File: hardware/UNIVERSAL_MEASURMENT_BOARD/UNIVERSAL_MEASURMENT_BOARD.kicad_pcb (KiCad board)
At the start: 2 copper layers, 68 parts, among them J10 2604-1104, J2 2606-1110_010-000, U1 ADS8863IDGS, U10 TPS54202HDDCR, U12 TPS54202HDDCR, U13 L7805ABD2T-TR, U14 ADM3055EBRIZ-RL, U15 TLV76133KVUR, U16 TLV76133KVUR, U2 LT3471EDD#PBF, U3 CD4067BM96, U4 PGA280AIPW, U5 CD4067BM96, U6 STM32G484RET3, U7 L7812ABD2T-TR, U8 MC7815BDTRKG, Y1 ECS-1612MV

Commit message: final schematic review corrections
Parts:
- removed D41, D46: 3.6V/400W, Package_TO_SOT_SMD:SOT-23-6
- removed D43: BZX84C5V6, Package_TO_SOT_SMD:SOT-23
- removed D45: BZX84C3V6-E3-08, Package_TO_SOT_SMD:SOT-23
- removed J10: 2604-1104, 2604-1104:26041104
- added C11: 100nF, Capacitor_SMD:C_0805_2012Metric, F.Cu at (165.4, 110.4)
- added C12: 1uF, Capacitor_SMD:C_0805_2012Metric, F.Cu at (160.2, 45.3)
- added C34: 100nF, Capacitor_SMD:C_0805_2012Metric, F.Cu at (169.1, 57.3)
- added C35: 1uF, Capacitor_SMD:C_0805_2012Metric, F.Cu at (169.1, 60.3)
- added C36: 1uF, Capacitor_SMD:C_0805_2012Metric, F.Cu at (169.1, 63.4)
- added C37: 100nF, Capacitor_SMD:C_0805_2012Metric, F.Cu at (173.5, 45.3)
- added C39: 1uF, Capacitor_SMD:C_0805_2012Metric, F.Cu at (173.5, 51.3)
- added C5: 100nF, Capacitor_SMD:C_0805_2012Metric, F.Cu at (165.4, 98.4)
- added C7: 470nF, Capacitor_SMD:C_0805_2012Metric, F.Cu at (165.4, 101.4)
- added C8: 470nF, Capacitor_SMD:C_0805_2012Metric, F.Cu at (165.4, 104.4)
- added C9: 470nF, Capacitor_SMD:C_0805_2012Metric, F.Cu at (165.4, 107.4)
- added J1: 2606-1110_010-000, 2601-1110:26011110, F.Cu at (93.3, 50.0)
- added J3: 2606-1110_010-000, 2601-1110:26011110, F.Cu at (93.3, 90.5)
- added J4: 2606-1110_010-000, 2601-1110:26011110, F.Cu at (93.3, 110.7)
- added J5: 2604-1104, 2601-1104:26011104, F.Cu at (133.7, 49.5)
- added U11: CD4097BM, CD4097BM:SOIC127P1030X265-24N, F.Cu at (156.8, 105.5)
- added U17: ESDS304DBVR, ESDS304DBVR:SOT95P280X145-5N, F.Cu at (131.6, 65.8)
- added U18: ESDS304DBVR, ESDS304DBVR:SOT95P280X145-5N, F.Cu at (131.6, 70.4)
- J2: footprint 2604-1110:26041110 -> 2601-1110:26011110
- U3: value CD4067BM96 -> MAX6063AEUR+T; footprint CD4067BM96:SOIC127P1030X265-24N -> MAX6063AEUR+T:SOT95P229X119-3N
- U5: value CD4067BM96 -> ISL21010CFH315Z-TK; footprint CD4067BM96:SOIC127P1030X265-24N -> ISL21010CFH315Z-TK:SOT95P237X112-3N
- moved U15 76.1 mm to (191.9, 48.6)
- moved U16 76.1 mm to (191.9, 58.2)
- moved U10 72.1 mm to (195.5, 87.2)
- moved U14 67.0 mm to (180.5, 126.6)
- moved C21 63.5 mm to (164.6, 48.3)
- moved C20 63.5 mm to (164.6, 45.3)
- moved C27 61.1 mm to (169.1, 45.3)
- moved C31 61.1 mm to (169.1, 51.3)
- moved C28 61.1 mm to (169.1, 48.3)
- moved U13 60.2 mm to (180.9, 75.2)
- moved U6 58.2 mm to (181.4, 104.1)
- moved C52 57.3 mm to (177.9, 51.3)
- moved C53 57.3 mm to (177.9, 54.3)
- moved C55 57.3 mm to (177.9, 57.3)
- moved C56 57.3 mm to (177.9, 60.3)
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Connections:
- net +12VA renamed +12V0A
- net +15V renamed +15V0
- net +15VF renamed +15V0F
- net +18V renamed +18V0
- net +7V renamed +7V0
- net -18V renamed -18V0
- net /can/RX renamed /can/CAN_RX
- net /can/TX renamed /can/CAN_TX
- C16 pad 1: +15VA -> +15V0A
- C28 pad 2: -15VA -> -15V0A
- C57 pad 1: +5VA -> +5V0A
- U1 pad 1: Net-(U1-REF) -> +3V0A
- U13 pad 3: +5VA -> +5V0A
- U3 pad 1: Net-(U3-OUT) -> +5V0A
- U3 pad 2: /connectors/A8P -> +3V0A
- U3 pad 3: /connectors/A7P -> GND
- U4 pad 10: Net-(U4-INN1) -> /mux & pga/NS
- U4 pad 11: -15VA -> Net-(U4-VSN)
- U4 pad 13: +3.3VA -> Net-(U4-DVDD)
- U4 pad 3: unconnected-(U4-VOCM-Pad3) -> 1V5A
- U4 pad 4: +3.3VA -> Net-(U4-VSOP)
- U4 pad 6: +15VA -> Net-(U4-VSP)
- U4 pad 9: Net-(U3-OUT) -> /mux & pga/PS
- U5 pad 1: Net-(U4-INN1) -> +3V3A
- U5 pad 2: /connectors/A8N -> +1V5A
- U5 pad 3: /connectors/A7N -> GND
- U6 pad 28: unconnected-(U6-VREF+-Pad28) -> 3V0A
- U6 pad 30: /mcu & adc/UART_RX_PROG -> /connectors/UART_RX_PROG
- U6 pad 56: /mcu & adc/SWO -> /connectors/SWO
- U6 pad 7: /mcu & adc/NRST -> /connectors/NRST
- U6 pad 9: /mcu & adc/UART_TX_PROG -> /connectors/UART_TX_PROG
- U8 pad 3: +15VA -> +15V0A

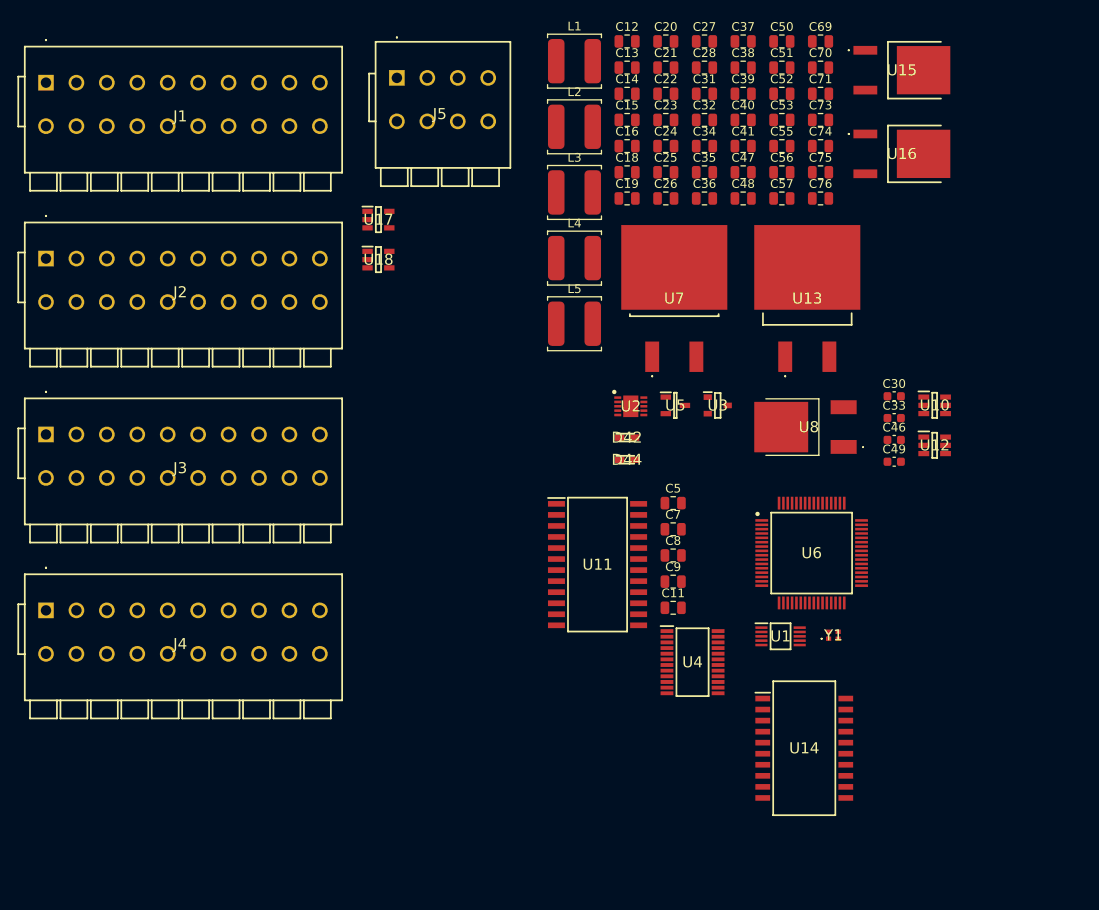
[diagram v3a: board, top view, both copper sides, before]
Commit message: added footprints
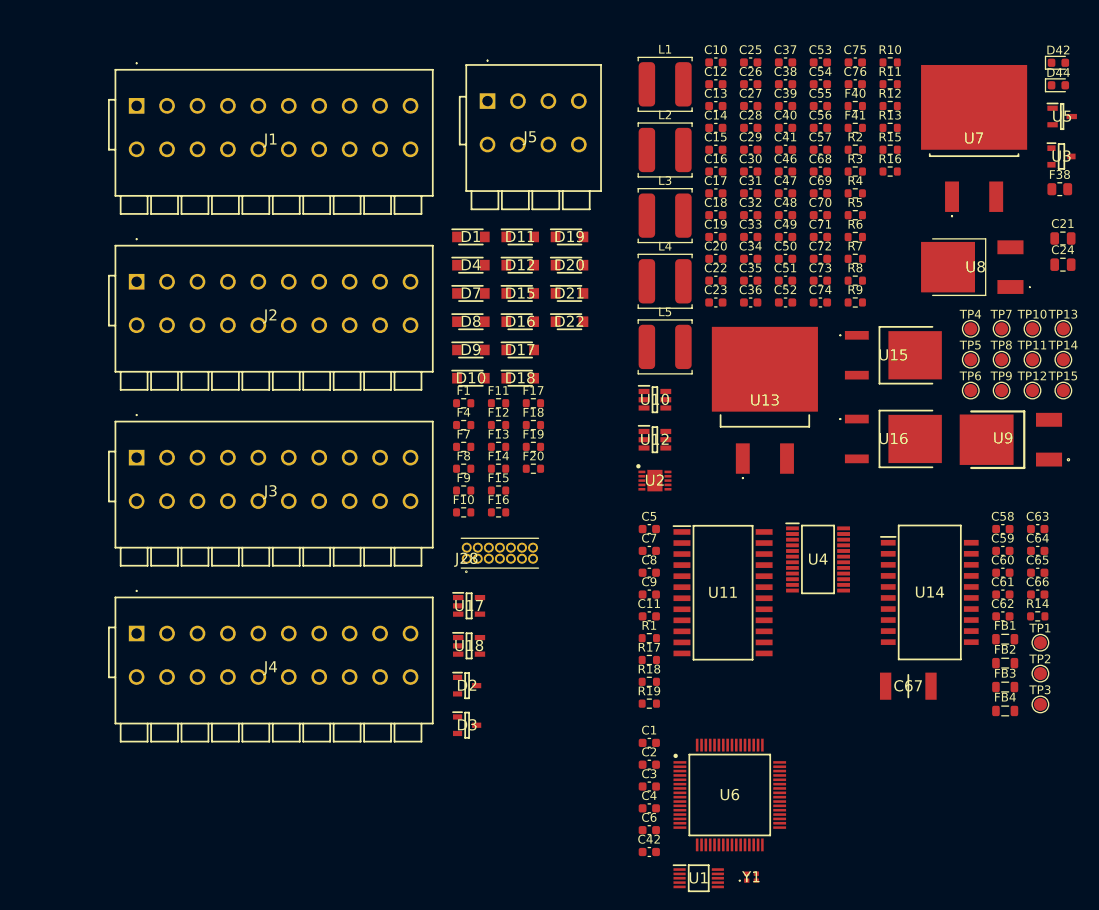
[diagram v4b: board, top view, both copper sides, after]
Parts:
- added C1: 100nF, Capacitor_SMD:C_0603_1608Metric, F.Cu at (162.7, 126.0)
- added C10: 220uF, Capacitor_SMD:C_0603_1608Metric, F.Cu at (170.4, 47.7)
- added C17: 1uF, Capacitor_SMD:C_0603_1608Metric, F.Cu at (170.4, 62.8)
- added C2: 100nF, Capacitor_SMD:C_0603_1608Metric, F.Cu at (162.7, 128.5)
- added C29: 1uF, Capacitor_SMD:C_0603_1608Metric, F.Cu at (174.4, 57.8)
- added C3: 10nF, Capacitor_SMD:C_0603_1608Metric, F.Cu at (162.7, 131.0)
- added C4: 100nF, Capacitor_SMD:C_0603_1608Metric, F.Cu at (162.7, 133.5)
- added C42: 100nF, Capacitor_SMD:C_0603_1608Metric, F.Cu at (162.7, 138.5)
- added C54: 10uF, Capacitor_SMD:C_0603_1608Metric, F.Cu at (182.4, 50.2)
- added C58: 47uF, Capacitor_SMD:C_0603_1608Metric, F.Cu at (203.4, 101.4)
- added C59: 47uF, Capacitor_SMD:C_0603_1608Metric, F.Cu at (203.4, 103.9)
- added C6: 10pF, Capacitor_SMD:C_0603_1608Metric, F.Cu at (162.7, 136.0)
- added C60: 47uF, Capacitor_SMD:C_0603_1608Metric, F.Cu at (203.4, 106.4)
- added C61: 47uF, Capacitor_SMD:C_0603_1608Metric, F.Cu at (203.4, 108.9)
- added C62: 100nF, Capacitor_SMD:C_0603_1608Metric, F.Cu at (203.4, 111.4)
- added C63: 100nF, Capacitor_SMD:C_0603_1608Metric, F.Cu at (207.4, 101.4)
- added C64: 10nF, Capacitor_SMD:C_0603_1608Metric, F.Cu at (207.4, 103.9)
- added C65: 10nF, Capacitor_SMD:C_0603_1608Metric, F.Cu at (207.4, 106.4)
- added C66: 100nF, Capacitor_SMD:C_0603_1608Metric, F.Cu at (207.4, 108.9)
- added C67: 4.7nF/Y2, S252B222K502CT:CAPC5728X280N, F.Cu at (192.5, 119.5)
- added C68: 10uF, Capacitor_SMD:C_0603_1608Metric, F.Cu at (182.4, 60.3)
- added C72: 10uF, Capacitor_SMD:C_0603_1608Metric, F.Cu at (182.4, 70.3)
- added D1: ATV02W150-HF, ATV02W150-HF:SODFL3718X130N, F.Cu at (142.2, 67.8)
- added D10: ATV02W150-HF, ATV02W150-HF:SODFL3718X130N, F.Cu at (142.2, 84.0)
- added D11: ATV02W150-HF, ATV02W150-HF:SODFL3718X130N, F.Cu at (147.9, 67.8)
- added D12: ATV02W150-HF, ATV02W150-HF:SODFL3718X130N, F.Cu at (147.9, 71.0)
- added D15: ATV02W150-HF, ATV02W150-HF:SODFL3718X130N, F.Cu at (147.9, 74.3)
- added D16: ATV02W150-HF, ATV02W150-HF:SODFL3718X130N, F.Cu at (147.9, 77.5)
- added D17: ATV02W150-HF, ATV02W150-HF:SODFL3718X130N, F.Cu at (147.9, 80.8)
- added D18: ATV02W150-HF, ATV02W150-HF:SODFL3718X130N, F.Cu at (147.9, 84.0)
- added D19: ATV02W150-HF, ATV02W150-HF:SODFL3718X130N, F.Cu at (153.5, 67.8)
- added D2: PESD5V0L2BT,215, PESD5V0L2BT,215:SOT95P230X110-3N, F.Cu at (141.8, 119.4)
- added D20: ATV02W150-HF, ATV02W150-HF:SODFL3718X130N, F.Cu at (153.5, 71.0)
- added D21: ATV02W150-HF, ATV02W150-HF:SODFL3718X130N, F.Cu at (153.5, 74.3)
- added D22: ATV02W150-HF, ATV02W150-HF:SODFL3718X130N, F.Cu at (153.5, 77.5)
- added D3: PESD5V0L2BT,215, PESD5V0L2BT,215:SOT95P230X110-3N, F.Cu at (141.8, 123.9)
- added D4: ATV02W150-HF, ATV02W150-HF:SODFL3718X130N, F.Cu at (142.2, 71.0)
- added D7: ATV02W150-HF, ATV02W150-HF:SODFL3718X130N, F.Cu at (142.2, 74.3)
- added D8: ATV02W150-HF, ATV02W150-HF:SODFL3718X130N, F.Cu at (142.2, 77.5)
- added D9: ATV02W150-HF, ATV02W150-HF:SODFL3718X130N, F.Cu at (142.2, 80.8)
- added F1: 100mA, Resistor_SMD:R_0603_1608Metric, F.Cu at (141.4, 86.9)
- added F10: 100mA, Resistor_SMD:R_0603_1608Metric, F.Cu at (141.4, 99.5)
- added F11: 100mA, Resistor_SMD:R_0603_1608Metric, F.Cu at (145.4, 86.9)
- added F12: 100mA, Resistor_SMD:R_0603_1608Metric, F.Cu at (145.4, 89.4)
- added F13: 100mA, Resistor_SMD:R_0603_1608Metric, F.Cu at (145.4, 91.9)
- added F14: 100mA, Resistor_SMD:R_0603_1608Metric, F.Cu at (145.4, 94.4)
- added F15: 100mA, Resistor_SMD:R_0603_1608Metric, F.Cu at (145.4, 97.0)
- added F16: 100mA, Resistor_SMD:R_0603_1608Metric, F.Cu at (145.4, 99.5)
- added F17: 100mA, Resistor_SMD:R_0603_1608Metric, F.Cu at (149.4, 86.9)
- added F18: 100mA, Resistor_SMD:R_0603_1608Metric, F.Cu at (149.4, 89.4)
- added F19: 100mA, Resistor_SMD:R_0603_1608Metric, F.Cu at (149.4, 91.9)
- added F20: 100mA, Resistor_SMD:R_0603_1608Metric, F.Cu at (149.4, 94.4)
- added F38: 1,5A, Resistor_SMD:R_0805_2012Metric, F.Cu at (209.9, 62.3)
- added F4: 100mA, Resistor_SMD:R_0603_1608Metric, F.Cu at (141.4, 89.4)
- added F40: 300mA, Resistor_SMD:R_0603_1608Metric, F.Cu at (186.4, 52.7)
- added F41: 300mA, Resistor_SMD:R_0603_1608Metric, F.Cu at (186.4, 55.2)
- added F7: 100mA, Resistor_SMD:R_0603_1608Metric, F.Cu at (141.4, 91.9)
- added F8: 100mA, Resistor_SMD:R_0603_1608Metric, F.Cu at (141.4, 94.4)
- added F9: 100mA, Resistor_SMD:R_0603_1608Metric, F.Cu at (141.4, 97.0)
- added FB1: 2K@100MHz, Inductor_SMD:L_0805_2012Metric, F.Cu at (203.6, 114.0)
- added FB2: 2K@100MHz, Inductor_SMD:L_0805_2012Metric, F.Cu at (203.6, 116.8)
- added FB3: 2K@100MHz, Inductor_SMD:L_0805_2012Metric, F.Cu at (203.6, 119.5)
- added FB4: 2K@100MHz, Inductor_SMD:L_0805_2012Metric, F.Cu at (203.6, 122.3)
- added J28: FTSH-107-01-L-D-K, FTSH-107-01-L-D-K:FTSH-107-XX-YYY-D-K, F.Cu at (141.7, 104.8)
- added R1: 22R, Resistor_SMD:R_0603_1608Metric, F.Cu at (162.7, 113.9)
- added R10: 649kR, Resistor_SMD:R_0603_1608Metric, F.Cu at (190.4, 47.7)
- added R11: 243kR, Resistor_SMD:R_0603_1608Metric, F.Cu at (190.4, 50.2)
- added R12: 64.9kR, Resistor_SMD:R_0603_1608Metric, F.Cu at (190.4, 52.7)
- added R13: 10kR, Resistor_SMD:R_0603_1608Metric, F.Cu at (190.4, 55.2)
- added R14: 100kR, Resistor_SMD:R_0603_1608Metric, F.Cu at (207.4, 111.4)
- added R15: 15kR, Resistor_SMD:R_0603_1608Metric, F.Cu at (190.4, 57.8)
- added R16: 274kR, Resistor_SMD:R_0603_1608Metric, F.Cu at (190.4, 60.3)
- added R17: 22R, Resistor_SMD:R_0603_1608Metric, F.Cu at (162.7, 116.4)
- added R18: 10R, Resistor_SMD:R_0603_1608Metric, F.Cu at (162.7, 119.0)
- added R19: 10R, Resistor_SMD:R_0603_1608Metric, F.Cu at (162.7, 121.5)
- added R2: 11kR, Resistor_SMD:R_0603_1608Metric, F.Cu at (186.4, 57.8)
- added R3: 11kR, Resistor_SMD:R_0603_1608Metric, F.Cu at (186.4, 60.3)
- added R4: 255kR, Resistor_SMD:R_0603_1608Metric, F.Cu at (186.4, 62.8)
- added R5: 15kR, Resistor_SMD:R_0603_1608Metric, F.Cu at (186.4, 65.3)
- added R6: 681kR, Resistor_SMD:R_0603_1608Metric, F.Cu at (186.4, 67.8)
- added R7: -R, Resistor_SMD:R_0603_1608Metric, F.Cu at (186.4, 70.3)
- added R8: 73.2kR, Resistor_SMD:R_0603_1608Metric, F.Cu at (186.4, 72.8)
- added R9: -R, Resistor_SMD:R_0603_1608Metric, F.Cu at (186.4, 75.3)
- added TP1: C5V, TestPoint:TestPoint_Pad_D1.5mm, F.Cu at (207.7, 114.5)
- added TP10: 12VA, TestPoint:TestPoint_Pad_D1.5mm, F.Cu at (206.8, 78.3)
- added TP11: 5VA, TestPoint:TestPoint_Pad_D1.5mm, F.Cu at (206.8, 81.9)
- added TP12: 3V3A, TestPoint:TestPoint_Pad_D1.5mm, F.Cu at (206.8, 85.5)
- added TP13: 3V3, TestPoint:TestPoint_Pad_D1.5mm, F.Cu at (210.3, 78.3)
- added TP14: 3V0A, TestPoint:TestPoint_Pad_D1.5mm, F.Cu at (210.3, 81.9)
- added TP15: 1V5A, TestPoint:TestPoint_Pad_D1.5mm, F.Cu at (210.3, 85.5)
- added TP2: C3V, TestPoint:TestPoint_Pad_D1.5mm, F.Cu at (207.7, 118.0)
- added TP3: CVISO, TestPoint:TestPoint_Pad_D1.5mm, F.Cu at (207.7, 121.5)
- added TP4: M15V, TestPoint:TestPoint_Pad_D1.5mm, F.Cu at (199.7, 78.3)
- added TP5: 18V, TestPoint:TestPoint_Pad_D1.5mm, F.Cu at (199.7, 81.9)
- added TP6: -18V, TestPoint:TestPoint_Pad_D1.5mm, F.Cu at (199.7, 85.5)
- added TP7: 7V, TestPoint:TestPoint_Pad_D1.5mm, F.Cu at (203.2, 78.3)
- added TP8: 15VA, TestPoint:TestPoint_Pad_D1.5mm, F.Cu at (203.2, 81.9)
- added TP9: -15VA, TestPoint:TestPoint_Pad_D1.5mm, F.Cu at (203.2, 85.5)
- added U9: MC79M15CDTRKG, MC79M15CDTRKG:DPAK__SINGLE-GAUGE__TO-252_369C__ISSUE_F, F.Cu at (199.7, 91.1)
- C11, C12, C13, C14, C15, C16, C18, C19, C20, C22, C23, C25, C26, C27, C28, C31, C32, C34, C35, C36, C37, C38, C39, C40, C41, C47, C48, C5, C50, C51, C52, C53, C55, C56, C57, C69, C7, C70, C71, C73, C74, C75, C76, C8, C9: footprint Capacitor_SMD:C_0805_2012Metric -> Capacitor_SMD:C_0603_1608Metric
- D42, D44: footprint CDBU0340:DIOM179X85N -> Diode_SMD:D_0603_1608Metric
- moved D42 65.7 mm to (209.8, 47.8)
- moved D44 65.7 mm to (209.8, 50.3)
- moved U5 55.5 mm to (210.2, 53.9)
- moved C21 49.7 mm to (210.3, 68.0)
- moved U3 48.8 mm to (210.1, 58.5)
- moved C24 47.7 mm to (210.3, 71.0)
- moved U17 45.6 mm to (142.0, 110.2)
- moved U18 45.6 mm to (142.0, 114.8)
- moved U7 39.1 mm to (200.1, 56.2)
- moved C46 33.3 mm to (178.4, 60.3)
- moved U15 32.8 mm to (190.9, 81.4)
- moved U16 32.8 mm to (190.9, 91.0)
- moved U10 32.2 mm to (163.3, 86.5)
- moved U12 32.2 mm to (163.3, 91.1)
- moved C30 30.7 mm to (174.4, 60.3)
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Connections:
- net Net-(J5A-1.2) renamed +24V0

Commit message: first outcom of pcb design
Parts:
- removed D20, D21, D22: ATV02W150-HF, ATV02W150-HF:SODFL3718X130N
- removed D42, D44: CDBU0340, Diode_SMD:D_0603_1608Metric
- removed F20: 100mA, Resistor_SMD:R_0603_1608Metric
- removed F38: 1,5A, Resistor_SMD:R_0805_2012Metric
- removed F40, F41: 300mA, Resistor_SMD:R_0603_1608Metric
- removed J28: FTSH-107-01-L-D-K, FTSH-107-01-L-D-K:FTSH-107-XX-YYY-D-K
- removed L4: 10uH, Inductor_SMD:L_TDK_VLS6045EX_VLS6045AF
- removed L5: 15uH, Inductor_SMD:L_TDK_VLS6045EX_VLS6045AF
- removed TP13: 3V3, TestPoint:TestPoint_Pad_D1.5mm
- removed TP14: 3V0A, TestPoint:TestPoint_Pad_D1.5mm
- removed the U4 at (182.1, 104.9)
- added C43: 330nF, REST:C_0603_1608Metric, F.Cu at (94.8, 90.6)
- added C44: 330nF, REST:C_0603_1608Metric, F.Cu at (107.7, 90.6)
- added C45: 330nF, REST:C_0603_1608Metric, F.Cu at (134.0, 104.9)
- added C77: 100nF, REST:C_0603_1608Metric, F.Cu at (107.9, 137.0)
- added C78: 100nF, REST:C_0603_1608Metric, F.Cu at (94.5, 137.0)
- added C79: 100nF, REST:C_0603_1608Metric, F.Cu at (107.9, 139.3)
- added D13: ATV02W150-HF, ATV02W150-HF:SODFL3718X130N, F.Cu at (112.8, 159.1)
- added D14: ATV02W150-HF, ATV02W150-HF:SODFL3718X130N, F.Cu at (112.8, 173.1)
- added D5: ATV02W150-HF, ATV02W150-HF:SODFL3718X130N, F.Cu at (89.7, 126.7)
- added D6: ATV02W150-HF, ATV02W150-HF:SODFL3718X130N, F.Cu at (89.7, 144.2)
- added F2: 1,5A, REST:F_0805_2012Metric, F.Cu at (94.3, 66.1)
- added F3: 300mA, REST:F_0603_1608Metric, F.Cu at (92.3, 75.1)
- added F5: 100mA, REST:F_1206_3216Metric, F.Cu at (89.7, 119.7)
- added F6: 100mA, REST:F_1206_3216Metric, F.Cu at (89.7, 133.7)
- added J6: Conn_01x01_Socket, REST:SolderWire-0.1sqmm_1x01_D0.4mm_OD1mm_Relief2x, F.Cu at (105.7, 65.8)
- added J7: Conn_01x01_Socket, REST:SolderWire-0.1sqmm_1x01_D0.4mm_OD1mm_Relief2x, F.Cu at (99.7, 65.8)
- added J8: 2606-1110_010-000, 2601-1110:26011110, F.Cu at (125.9, 167.7)
- added J9: 2606-1110_010-000, 2601-1110:26011110, F.Cu at (125.9, 131.2)
- added L6: ASPIAIG-S8050-221M-T, ASPIAIG-S8050-221M-T:INDPM8080X520N, F.Cu at (87.2, 84.2)
- added REF**: MountingHole_3.2mm_M3_Pad_Via, REST:MountingHole_3.2mm_M3_Pad_Via, F.Cu at (132.2, 193.8)
- added REF**: Screw_Generic_2.0x3.0mm_SilkScreen, Symbol:Screw_Generic_2.0x3.0mm_SilkScreen, F.Cu at (95.2, 143.8)
- added REF**: MountingHole_3.2mm_M3_Pad_Via, REST:MountingHole_3.2mm_M3_Pad_Via, F.Cu at (132.2, 66.8)
- added REF**: MountingHole_3.2mm_M3_Pad_Via, REST:MountingHole_3.2mm_M3_Pad_Via, F.Cu at (101.2, 143.8)
- added REF**: MountingHole_3.2mm_M3_Pad_Via, REST:MountingHole_3.2mm_M3_Pad_Via, F.Cu at (70.2, 193.8)
- added REF**: MountingHole_3.2mm_M3_Pad_Via, REST:MountingHole_3.2mm_M3_Pad_Via, F.Cu at (70.2, 66.8)
- added U11: L7812ABD2T-TR, L7812ABD2T-TR:L7812ABD2TTR, F.Cu at (109.2, 99.6)
- C1, C11, C19, C2, C22, C32, C38, C40, C49, C5, C6, C62, C75, C8, C9: footprint Capacitor_SMD:C_0603_1608Metric -> REST:C_0603_1608Metric
- C10: value 220uF -> 470nF; footprint Capacitor_SMD:C_0603_1608Metric -> REST:C_0603_1608Metric
- C12: value 1uF -> 10uF; footprint Capacitor_SMD:C_0603_1608Metric -> REST:C_0805_2012Metric
- C13: value 100nF -> 22uF; footprint Capacitor_SMD:C_0603_1608Metric -> REST:C_0805_2012Metric
- C14, C26, C47, C48, C50, C73, C76: value 22uF -> 100nF; footprint Capacitor_SMD:C_0603_1608Metric -> REST:C_0603_1608Metric
- C15: value 330nF -> 22uF; footprint Capacitor_SMD:C_0603_1608Metric -> REST:C_0603_1608Metric
- C16: value 220nF -> 22uF; footprint Capacitor_SMD:C_0603_1608Metric -> REST:C_0805_2012Metric
- C17, C35, C36, C39: value 1uF -> 22uF; footprint Capacitor_SMD:C_0603_1608Metric -> REST:C_0603_1608Metric
- C18, C68: value 10uF -> 100nF; footprint Capacitor_SMD:C_0603_1608Metric -> REST:C_0603_1608Metric
- C20, C23: value 1uF -> 100nF; footprint Capacitor_SMD:C_0603_1608Metric -> REST:C_0603_1608Metric
- C21: value 4.7uF -> 1uF; footprint Capacitor_SMD:C_0805_2012Metric -> REST:C_0603_1608Metric
- C24: value 10uF -> 1uF; footprint Capacitor_SMD:C_0805_2012Metric -> REST:C_0805_2012Metric
- C25: value 75pF -> 22uF; footprint Capacitor_SMD:C_0603_1608Metric -> REST:C_0805_2012Metric
- C27: value 330nF -> 75pF; footprint Capacitor_SMD:C_0603_1608Metric -> REST:C_0603_1608Metric
- C28: value 220nF -> 100nF; footprint Capacitor_SMD:C_0603_1608Metric -> REST:C_0603_1608Metric
- C29: value 1uF -> 22uF; footprint Capacitor_SMD:C_0603_1608Metric -> REST:C_0805_2012Metric
- C3: value 10nF -> 100nF; footprint Capacitor_SMD:C_0603_1608Metric -> REST:C_0603_1608Metric
- C30: value 100nF -> 10uF; footprint Capacitor_SMD:C_0603_1608Metric -> REST:C_0805_2012Metric
- C31: value 22uF -> 4.7uF; footprint Capacitor_SMD:C_0603_1608Metric -> REST:C_0805_2012Metric
- C33: value 100nF -> 220uF; footprint Capacitor_SMD:C_0603_1608Metric -> REST:CP_Elec_8x10
- C34, C37, C53: value 100nF -> 22uF; footprint Capacitor_SMD:C_0603_1608Metric -> REST:C_0603_1608Metric
- C4, C71: value 100nF -> 10nF; footprint Capacitor_SMD:C_0603_1608Metric -> REST:C_0603_1608Metric
- C41: value 22uF -> 330nF; footprint Capacitor_SMD:C_0603_1608Metric -> REST:C_0603_1608Metric
- C42, C46: value 100nF -> 330nF; footprint Capacitor_SMD:C_0603_1608Metric -> REST:C_0603_1608Metric
- C51: value 22uF -> 220nF; footprint Capacitor_SMD:C_0603_1608Metric -> REST:C_0603_1608Metric
- C52: value 330nF -> 220nF; footprint Capacitor_SMD:C_0603_1608Metric -> REST:C_0603_1608Metric
- C54: footprint Capacitor_SMD:C_0603_1608Metric -> REST:CP_Elec_4x5.8
- C55: value 22uF -> 10uF; footprint Capacitor_SMD:C_0603_1608Metric -> REST:CP_Elec_4x5.8
- C56: value 330nF -> 10uF; footprint Capacitor_SMD:C_0603_1608Metric -> REST:CP_Elec_4x5.8
- C57: value 100nF -> 1uF; footprint Capacitor_SMD:C_0603_1608Metric -> REST:CP_Elec_4x5.4
- C58: value 47uF -> 1uF; footprint Capacitor_SMD:C_0603_1608Metric -> REST:CP_Elec_4x5.4
- C59, C60: value 47uF -> 1uF; footprint Capacitor_SMD:C_0603_1608Metric -> REST:C_0603_1608Metric
- C61: value 47uF -> 100nF; footprint Capacitor_SMD:C_0603_1608Metric -> REST:C_0603_1608Metric
- C63: value 100nF -> 1uF; footprint Capacitor_SMD:C_0603_1608Metric -> REST:C_0603_1608Metric
- C64: value 10nF -> 1uF; footprint Capacitor_SMD:C_0603_1608Metric -> REST:C_0603_1608Metric
- C65: value 10nF -> 47uF; footprint Capacitor_SMD:C_0603_1608Metric -> REST:C_0603_1608Metric
- C66: value 100nF -> 47uF; footprint Capacitor_SMD:C_0603_1608Metric -> REST:C_0603_1608Metric
- C67: value 4.7nF/Y2 -> 100nF; footprint S252B222K502CT:CAPC5728X280N -> REST:C_0603_1608Metric
- C69: value 22uF -> 10nF; footprint Capacitor_SMD:C_0603_1608Metric -> REST:C_0603_1608Metric
- C7: value 470nF -> 100nF; footprint Capacitor_SMD:C_0603_1608Metric -> REST:C_0603_1608Metric
- C70: value 330nF -> 4.7nF/Y2; footprint Capacitor_SMD:C_0603_1608Metric -> S252B222K502CT:CAPC5728X280N
- C72: value 10uF -> 47uF; footprint Capacitor_SMD:C_0603_1608Metric -> REST:C_0603_1608Metric
- C74: value 330nF -> 47uF; footprint Capacitor_SMD:C_0603_1608Metric -> REST:C_0603_1608Metric
- D1: value ATV02W150-HF -> CDBU0340; footprint ATV02W150-HF:SODFL3718X130N -> REST:D_0603_1608Metric
- D11: value ATV02W150-HF -> PESD5V0L2BT,215; footprint ATV02W150-HF:SODFL3718X130N -> PESD5V0L2BT,215:SOT95P230X110-3N
- D2: value PESD5V0L2BT,215 -> CDBU0340; footprint PESD5V0L2BT,215:SOT95P230X110-3N -> REST:D_0603_1608Metric
- D3: value PESD5V0L2BT,215 -> ATV02W150-HF; footprint PESD5V0L2BT,215:SOT95P230X110-3N -> ATV02W150-HF:SODFL3718X130N
- F1: value 100mA -> 300mA; footprint Resistor_SMD:R_0603_1608Metric -> REST:F_0603_1608Metric
- F10, F11, F12, F13, F14, F15, F16, F17, F18, F19, F4, F7, F8, F9: footprint Resistor_SMD:R_0603_1608Metric -> REST:F_1206_3216Metric
- FB1, FB2, FB3, FB4: footprint Inductor_SMD:L_0805_2012Metric -> REST:L_0805_2012Metric
- J1: value 2606-1110_010-000 -> FTSH-107-01-L-D-K; footprint 2601-1110:26011110 -> FTSH-107-01-L-D-K:FTSH-107-XX-YYY-D-K
- J4: value 2606-1110_010-000 -> Conn_01x01_Socket; footprint 2601-1110:26011110 -> REST:SolderWire-0.1sqmm_1x01_D0.4mm_OD1mm_Relief2x
- J5: value 2604-1104 -> Conn_01x01_Socket; footprint 2601-1104:26011104 -> REST:SolderWire-0.1sqmm_1x01_D0.4mm_OD1mm_Relief2x
- L1: value 2.2uH -> PM3604-5-RC; footprint Inductor_SMD:L_TDK_VLS6045EX_VLS6045AF -> PM3604-5-RC:PM3604-5-RC
- L2: value 68uH/1.4A -> 74408943100; footprint Inductor_SMD:L_TDK_VLS6045EX_VLS6045AF -> 74408943100:WE-SPC_48XX78
- L3: value 68uH/1.4A -> 74437349560; footprint Inductor_SMD:L_TDK_VLS6045EX_VLS6045AF -> 74437349560:74437349560
- R1: value 22R -> 10R; footprint Resistor_SMD:R_0603_1608Metric -> REST:R_0603_1608Metric
- R10: value 649kR -> 73.2kR; footprint Resistor_SMD:R_0603_1608Metric -> REST:R_0603_1608Metric
- R11: footprint Resistor_SMD:R_0603_1608Metric -> REST:R_0603_1608Metric
- R12: value 64.9kR -> 10kR; footprint Resistor_SMD:R_0603_1608Metric -> REST:R_0603_1608Metric
- R13: value 10kR -> 255kR; footprint Resistor_SMD:R_0603_1608Metric -> REST:R_0603_1608Metric
- R14: value 100kR -> -R; footprint Resistor_SMD:R_0603_1608Metric -> REST:R_0603_1608Metric
- R15: value 15kR -> -R; footprint Resistor_SMD:R_0603_1608Metric -> REST:R_0603_1608Metric
- R16: value 274kR -> 15kR; footprint Resistor_SMD:R_0603_1608Metric -> REST:R_0603_1608Metric
- R17: value 22R -> 15kR; footprint Resistor_SMD:R_0603_1608Metric -> REST:R_0603_1608Metric
- R18: value 10R -> 274kR; footprint Resistor_SMD:R_0603_1608Metric -> REST:R_0603_1608Metric
- R19: value 10R -> 100kR; footprint Resistor_SMD:R_0603_1608Metric -> REST:R_0603_1608Metric
- R2: value 11kR -> 10R; footprint Resistor_SMD:R_0603_1608Metric -> REST:R_0603_1608Metric
- R3: value 11kR -> 22R; footprint Resistor_SMD:R_0603_1608Metric -> REST:R_0603_1608Metric
- R4: value 255kR -> 22R; footprint Resistor_SMD:R_0603_1608Metric -> REST:R_0603_1608Metric
- R5: value 15kR -> 11kR; footprint Resistor_SMD:R_0603_1608Metric -> REST:R_0603_1608Metric
- R6: value 681kR -> 649kR; footprint Resistor_SMD:R_0603_1608Metric -> REST:R_0603_1608Metric
- R7: value -R -> 681kR; footprint Resistor_SMD:R_0603_1608Metric -> REST:R_0603_1608Metric
- R8: value 73.2kR -> 64.9kR; footprint Resistor_SMD:R_0603_1608Metric -> REST:R_0603_1608Metric
- R9: value -R -> 11kR; footprint Resistor_SMD:R_0603_1608Metric -> REST:R_0603_1608Metric
- TP1: value C5V -> M15V; footprint TestPoint:TestPoint_Pad_D1.5mm -> REST:TestPoint_Pad_D1.5mm; moved to B.Cu
- TP10: value 12VA -> -15VA; footprint TestPoint:TestPoint_Pad_D1.5mm -> REST:TestPoint_Pad_D1.5mm; moved to B.Cu
- TP11: value 5VA -> 1V5A; footprint TestPoint:TestPoint_Pad_D1.5mm -> REST:TestPoint_Pad_D1.5mm; moved to B.Cu
- TP12: value 3V3A -> 3V0A; footprint TestPoint:TestPoint_Pad_D1.5mm -> REST:TestPoint_Pad_D1.5mm; moved to B.Cu
- TP15: value 1V5A -> CVISO; footprint TestPoint:TestPoint_Pad_D1.5mm -> REST:TestPoint_Pad_D1.5mm; moved to B.Cu
- TP2: value C3V -> -18V; footprint TestPoint:TestPoint_Pad_D1.5mm -> REST:TestPoint_Pad_D1.5mm; moved to B.Cu
- TP3: value CVISO -> 7V; footprint TestPoint:TestPoint_Pad_D1.5mm -> REST:TestPoint_Pad_D1.5mm; moved to B.Cu
- TP4: value M15V -> 18V; footprint TestPoint:TestPoint_Pad_D1.5mm -> REST:TestPoint_Pad_D1.5mm; moved to B.Cu
- TP5: value 18V -> 3V3; footprint TestPoint:TestPoint_Pad_D1.5mm -> REST:TestPoint_Pad_D1.5mm; moved to B.Cu
- TP6: value -18V -> 3V3A; footprint TestPoint:TestPoint_Pad_D1.5mm -> REST:TestPoint_Pad_D1.5mm; moved to B.Cu
- TP7: value 7V -> 5VA; footprint TestPoint:TestPoint_Pad_D1.5mm -> REST:TestPoint_Pad_D1.5mm; moved to B.Cu
- TP8: value 15VA -> 12VA; footprint TestPoint:TestPoint_Pad_D1.5mm -> REST:TestPoint_Pad_D1.5mm; moved to B.Cu
- TP9: value -15VA -> 15VA; footprint TestPoint:TestPoint_Pad_D1.5mm -> REST:TestPoint_Pad_D1.5mm; moved to B.Cu
- U1: value ADS8863IDGS -> STM32G484RET3; footprint ADS8863IDGS:SOP50P490X110-10N -> STM32G484RET3:QFP50P1200X1200X160-64N
- U10: value TPS54202HDDCR -> L7805ABD2T-TR; footprint TPS54202HDDCR:SOT95P280X110-6N -> L7805ABD2T-TR:L7805ABD2TTR
- U12: value TPS54202HDDCR -> L78L15ACD13TR; footprint TPS54202HDDCR:SOT95P280X110-6N -> LP358DR:SOIC127P600X175-8N
- U13: value L7805ABD2T-TR -> L79L15ACD13TR; footprint L7805ABD2T-TR:L7805ABD2TTR -> LP358DR:SOIC127P600X175-8N
- U14: value ADM3055EBRIZ-RL -> ISL21010CFH315Z-TK; footprint ADM3055EBRIZ-RL:SOIC127P1030X264-20N -> ISL21010CFH315Z-TK:SOT95P237X112-3N
- U15: value TLV76133KVUR -> ISL21010CFH330Z-TK; footprint TLV76133KVUR:TLV76133KVUR -> ISL21010CFH315Z-TK:SOT95P237X112-3N
- U16: value TLV76133KVUR -> ESDS304DBVR; footprint TLV76133KVUR:TLV76133KVUR -> ESDS304DBVR:SOT95P280X145-5N
- U18: value ESDS304DBVR -> ADM3055EBRIZ-RL; footprint ESDS304DBVR:SOT95P280X145-5N -> ADM3055EBRIZ-RL:SOIC127P1030X264-20N
- U2: value LT3471EDD#PBF -> ADS8863IDGS; footprint LT3471EDD#PBF:SON50P300X300X80-11N-D -> ADS8863IDGS:SOP50P490X110-10N
- U3: value MAX6063AEUR+T -> PGA280AIPW; footprint MAX6063AEUR+T:SOT95P229X119-3N -> PGA280AIPW:SOP65P640X120-24N
- U5: value ISL21010CFH315Z-TK -> TPS54202HDDCR; footprint ISL21010CFH315Z-TK:SOT95P237X112-3N -> TPS54202HDDCR:SOT95P280X110-6N
- U6: value STM32G484RET3 -> TPS54202HDDCR; footprint STM32G484RET3:QFP50P1200X1200X160-64N -> TPS54202HDDCR:SOT95P280X110-6N
- U7: value L7812ABD2T-TR -> LT3471EDD#PBF; footprint L7812ABD2T-TR:L7812ABD2TTR -> LT3471EDD#PBF:SON50P300X300X80-11N-D
- U8: value MC7815BDTRKG -> UA78M33CDCYRG3; footprint MC7815BDTRKG:NVD5117PLT4GVF01 -> UA78M33CDCYRG3:SOT230P700X180-4N
- U9: value MC79M15CDTRKG -> UA78M33CDCYRG3; footprint MC79M15CDTRKG:DPAK__SINGLE-GAUGE__TO-252_369C__ISSUE_F -> UA78M33CDCYRG3:SOT230P700X180-4N
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- renumbered U11 to U4
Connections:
- C10 pad 1: +15V0 -> Net-(U3-VSN)
- C11 pad 2: Net-(U4-DVDD) -> +15V0A
- C12 pad 1: +5V0A -> GND
- C12 pad 2: GND -> +15V0F
- C13 pad 2: +15V0F -> Net-(U5-VIN)
- C14 pad 1: +18V0 -> GND
- C14 pad 2: GND -> +15V0F
- C15 pad 1: +18V0 -> GND
- C15 pad 2: GND -> Net-(U6-VIN)
- C16 pad 1: +15V0A -> GND
- C16 pad 2: GND -> Net-(U5-VIN)
- C17 pad 1: +15V0A -> GND
- C17 pad 2: GND -> Net-(U6-VIN)
- C18 pad 2: +15V0F -> Net-(U5-VIN)
- C19 pad 2: Net-(U2-~{SHDN}/SS1) -> Net-(U7-~{SHDN}/SS1)
- C2 pad 1: +3V3A -> +3V3
- C20 pad 2: Net-(U2-~{SHDN}/SS2) -> Net-(U6-VIN)
- C21 pad 2: +18V0 -> Net-(U7-~{SHDN}/SS2)
- C22 pad 1: GND -> Net-(U5-BOOT)
- C22 pad 2: Net-(U2-FB1P) -> Net-(U5-SW)
- C23 pad 1: Net-(D44-A) -> Net-(U6-BOOT)
- C23 pad 2: Net-(U2-SW2) -> Net-(U6-SW)
- C24 pad 1: GND -> Net-(D2-A)
- C24 pad 2: -18V0 -> Net-(U7-SW2)
- C25 pad 1: -18V0 -> +15V0
- C25 pad 2: Net-(U2-FB2P) -> GND
- C26 pad 2: -18V0 -> Net-(U7-FB1P)
- C27 pad 1: GND -> -18V0
- C27 pad 2: -18V0 -> Net-(U7-FB2P)
- C28 pad 1: GND -> +7V0
- C28 pad 2: -15V0A -> GND
- C29 pad 1: GND -> +15V0
- C29 pad 2: -15V0A -> GND
- C30 pad 1: Net-(U10-BOOT) -> GND
- C30 pad 2: Net-(U10-SW) -> -18V0
- C31 pad 2: Net-(U10-VIN) -> +18V0
- C32 pad 1: GND -> +7V0
- C32 pad 2: Net-(U10-VIN) -> GND
- C33 pad 1: GND -> +15V0
- C33 pad 2: Net-(U10-VIN) -> GND
- C34 pad 1: +1V5A -> +7V0
- C35 pad 1: +1V5A -> +7V0
- C36 pad 1: +3V3A -> +7V0
- C37 pad 1: +3V0A -> +7V0
- C38 pad 1: +7V0 -> +15V0
- C39 pad 1: +3V0A -> +18V0
- C4 pad 1: +3V0A -> +3V3A
- C40 pad 1: +15V0 -> GND
- C40 pad 2: GND -> -18V0
- C42 pad 1: +3V3 -> +7V0
- C46 pad 1: Net-(U12-BOOT) -> GND
- C46 pad 2: Net-(U12-SW) -> -18V0
- C47 pad 1: GND -> +3V3
- C47 pad 2: Net-(U12-VIN) -> GND
- C48 pad 1: GND -> +3V3A
- C48 pad 2: Net-(U12-VIN) -> GND
- C49 pad 1: GND -> +5V0A
- C49 pad 2: Net-(U12-VIN) -> GND
- C5 pad 1: GND -> +3V0A
- C5 pad 2: +15V0A -> GND
- C50 pad 1: +15V0 -> +12V0A
- C51 pad 1: +15V0 -> +15V0A
- C52 pad 1: +15V0 -> GND
- C52 pad 2: GND -> -15V0A
- C53 pad 1: +12V0A -> +3V3
- C54 pad 1: +12V0A -> +3V3A
- C55 pad 1: +7V0 -> +5V0A
- C56 pad 1: +7V0 -> +12V0A
- C57 pad 1: +5V0A -> +15V0A
- C58 pad 1: Net-(U14-VISOOUT) -> GND
- C58 pad 2: Net-(U14-GNDISO) -> -15V0A
- C59 pad 1: VISO -> +3V3A
- C59 pad 2: BUS_GND -> GND
- C61 pad 1: Net-(U14-VCC) -> +1V5A
- C62 pad 1: Net-(U14-VCC) -> +3V0A
- C63 pad 1: +3V3 -> +1V5A
- C64 pad 1: Net-(U14-VIO) -> +3V0A
- C65 pad 1: VISO -> +5V0A
- C65 pad 2: BUS_GND -> GND
- C66 pad 1: VISO -> Net-(U18-VCC)
- C66 pad 2: BUS_GND -> GND
- C67 pad 1: BUS_GND -> Net-(U18-VCC)
- C68 pad 1: +5V0A -> +3V3
- C69 pad 1: +7V0 -> Net-(U18-VIO)
- C7 pad 2: Net-(U4-VSP) -> Net-(U3-DVDD)
- C70 pad 1: +7V0 -> GND_ISO
- C71 pad 1: +3V3A -> VISO
- C71 pad 2: GND -> GND_ISO
- C72 pad 1: +3V3A -> Net-(U18-VISOOUT)
- C72 pad 2: GND -> Net-(U18-GNDISO)
- C73 pad 1: +7V0 -> VISO
- C73 pad 2: GND -> GND_ISO
- C74 pad 1: +7V0 -> VISO
- C74 pad 2: GND -> GND_ISO
- C8 pad 1: Net-(U4-VSN) -> GND
- C8 pad 2: GND -> Net-(U3-VSOP)
- C9 pad 2: Net-(U4-VSOP) -> Net-(U3-VSP)
- D1 pad 1: /connectors/A1P -> +18V0
- D1 pad 2: GND -> Net-(D1-A)
- D10 pad 1: /connectors/A3N -> /connectors/A4N
- D11 pad 1: /connectors/A4P -> /can/CANH
- D11 pad 2: GND -> /can/CANL
- D12 pad 1: /connectors/A4N -> /connectors/A5P
- D15 pad 1: /connectors/A5P -> /connectors/A6N
- D16 pad 1: /connectors/A5N -> /connectors/A7P
- D17 pad 1: /connectors/A6P -> /connectors/A8P
- D18 pad 1: /connectors/A6N -> /connectors/A7N
- D19 pad 1: /connectors/A7P -> /connectors/A8N
- D2 pad 1: /can/CANL -> GND
- D2 pad 2: (no net) -> Net-(D2-A)
- D3 pad 1: (no net) -> /connectors/A1P
- D3 pad 2: /can/CANH -> GND
- D4 pad 1: /connectors/A1N -> /connectors/A2P
- D7 pad 1: /connectors/A2P -> /connectors/A3P
- D8 pad 1: /connectors/A2N -> /connectors/A4P
- D9 pad 1: /connectors/A3P -> /connectors/A3N
- F1 pad 1: +12V0 -> +15V0
- F1 pad 2: Net-(F1-Pad2) -> +15V0F
- F10 pad 1: +5V0 -> +12V0A
- F11 pad 1: +12V0 -> +5V0A
- F12 pad 1: +5V0 -> +12V0A
- F13 pad 1: +12V0 -> +5V0A
- F14 pad 1: +5V0 -> +12V0A
- F15 pad 1: +12V0 -> +5V0A
- F16 pad 1: +5V0 -> +12V0A
- F17 pad 1: +12V0 -> +5V0A
- F18 pad 1: +5V0 -> +12V0A
- F19 pad 1: +12V0 -> +5V0A
- F4 pad 1: +5V0 -> +12V0A
- F7 pad 1: +12V0 -> +5V0A
- F8 pad 1: +12V0 -> +12V0A
- F9 pad 1: +5V0 -> +5V0A
- FB1 pad 1: Net-(U14-VCC) -> Net-(U18-VCC)
- FB2 pad 1: VISO -> Net-(U18-VIO)
- FB2 pad 2: Net-(U14-VISOOUT) -> +3V3
- FB3 pad 1: Net-(U14-VIO) -> VISO
- FB3 pad 2: +3V3 -> Net-(U18-VISOOUT)
- FB4 pad 1: BUS_GND -> GND_ISO
- FB4 pad 2: Net-(U14-GNDISO) -> Net-(U18-GNDISO)
- J1 pad 1: Net-(F1-Pad2) -> unconnected-(J1-Pin_1-Pad1)
- J1 pad 10: GND -> unconnected-(J1-Pin_10-Pad10)
- J1 pad 11: (no net) -> GND
- J1 pad 12: (no net) -> /connectors/NRST
- J1 pad 13: (no net) -> /connectors/UART_RX_PROG
- J1 pad 14: (no net) -> /connectors/UART_TX_PROG
- J1 pad 2: Net-(F4-Pad2) -> unconnected-(J1-Pin_2-Pad2)
- J1 pad 3: /connectors/A1P -> +3V3
- J1 pad 4: /connectors/A1N -> /connectors/SWDIO
- J1 pad 6: Net-(F7-Pad2) -> /connectors/SWCLK
- J1 pad 7: Net-(F10-Pad2) -> GND
- J1 pad 8: /connectors/A2P -> /connectors/SWO
- J1 pad 9: /connectors/A2N -> unconnected-(J1-Pin_9-Pad9)
- J2 pad 1: Net-(F8-Pad2) -> Net-(F4-Pad2)
- J2 pad 2: Net-(F9-Pad2) -> Net-(F5-Pad2)
- J2 pad 3: /connectors/A3P -> /connectors/A1P
- J2 pad 4: /connectors/A3N -> /connectors/A1N
- J2 pad 6: Net-(F11-Pad2) -> Net-(F6-Pad2)
- J2 pad 7: Net-(F12-Pad2) -> Net-(F7-Pad2)
- J2 pad 8: /connectors/A4P -> /connectors/A2P
- J2 pad 9: /connectors/A4N -> /connectors/A2N
- J3 pad 1: Net-(F13-Pad2) -> Net-(F8-Pad2)
- J3 pad 2: Net-(F14-Pad2) -> Net-(F9-Pad2)
- J3 pad 3: /connectors/A5P -> /connectors/A3P
- J3 pad 4: /connectors/A5N -> /connectors/A3N
- J3 pad 6: Net-(F15-Pad2) -> Net-(F10-Pad2)
- J3 pad 7: Net-(F16-Pad2) -> Net-(F11-Pad2)
- J3 pad 8: /connectors/A6P -> /connectors/A4P
- J3 pad 9: /connectors/A6N -> /connectors/A4N
- J4 pad 1: Net-(F17-Pad2) -> +24V0
- J5 pad 1: +24V0 -> /can/CANH
- L1 pad 2: Net-(D42-A) -> Net-(U7-SW2)
- L2 pad 1: Net-(U10-SW) -> +15V0F
- L2 pad 2: +7V0 -> Net-(D1-A)
- L3 pad 1: Net-(U12-SW) -> Net-(U5-SW)
- R1 pad 1: -15V0A -> +3V3
- R1 pad 2: Net-(U4-VSN) -> Net-(U3-DVDD)
- R10 pad 1: Net-(U12-VIN) -> GND
- R10 pad 2: Net-(U12-EN) -> Net-(U6-EN)
- R11 pad 1: Net-(U12-FB) -> Net-(U5-FB)
- R12 pad 2: Net-(U12-EN) -> Net-(U5-FB)
- R13 pad 1: GND -> Net-(U7-FB1N)
- R13 pad 2: Net-(U12-FB) -> +18V0
- R14 pad 1: Net-(U14-RS) -> Net-(U6-FB)
- R14 pad 2: BUS_GND -> +7V0
- R15 pad 1: Net-(U2-FB2P) -> GND
- R15 pad 2: Net-(U2-FB1P) -> Net-(U6-FB)
- R16 pad 1: -18V0 -> Net-(U7-FB1N)
- R16 pad 2: Net-(U2-FB2P) -> GND
- R17 pad 1: +15V0A -> Net-(U7-FB2P)
- R17 pad 2: Net-(U4-VSP) -> Net-(U7-FB1P)
- R18 pad 1: +5V0A -> -18V0
- R18 pad 2: Net-(U4-VSOP) -> Net-(U7-FB2P)
- R19 pad 1: +3V3 -> Net-(U18-RS)
- R19 pad 2: Net-(U4-DVDD) -> GND_ISO
- R2 pad 1: +15V0F -> +5V0A
- R2 pad 2: Net-(U2-~{SHDN}/SS1) -> Net-(U3-VSOP)
- R3 pad 1: +15V0F -> +15V0A
- R3 pad 2: Net-(U2-~{SHDN}/SS2) -> Net-(U3-VSP)
- R4 pad 1: Net-(U2-FB1N) -> -15V0A
- R4 pad 2: +18V0 -> Net-(U3-VSN)
- R5 pad 1: Net-(U2-FB1N) -> +15V0F
- R5 pad 2: GND -> Net-(U7-~{SHDN}/SS1)
- R6 pad 1: Net-(U10-VIN) -> Net-(U5-VIN)
- R6 pad 2: Net-(U10-EN) -> Net-(U5-EN)
- R7 pad 1: Net-(U10-FB) -> Net-(U6-VIN)
- R7 pad 2: +7V0 -> Net-(U6-EN)
- R8 pad 2: Net-(U10-EN) -> Net-(U5-EN)
- R9 pad 1: GND -> +15V0F
- R9 pad 2: Net-(U10-FB) -> Net-(U7-~{SHDN}/SS2)
- TP1 pad 1: Net-(U14-VCC) -> +15V0
- TP10 pad 1: +12V0A -> -15V0A
- TP11 pad 1: +5V0A -> +1V5A
- TP12 pad 1: +3V3A -> +3V0A
- TP15 pad 1: +1V5A -> VISO
- TP2 pad 1: Net-(U14-VIO) -> -18V0
- TP3 pad 1: VISO -> +7V0
- TP4 pad 1: +15V0 -> +18V0
- TP5 pad 1: +18V0 -> +3V3
- TP6 pad 1: -18V0 -> +3V3A
- TP7 pad 1: +7V0 -> +5V0A
- TP8 pad 1: +15V0A -> +12V0A
- TP9 pad 1: -15V0A -> +15V0A
- U1 pad 1: +3V0A -> +3V3
- U1 pad 10: +3V3 -> unconnected-(U1-PC2-Pad10)
- U1 pad 2: +3V3A -> unconnected-(U1-PC13-Pad2)
- U1 pad 3: /mcu & adc/AINP -> unconnected-(U1-PC14-Pad3)
- U1 pad 4: /mcu & adc/AINN -> unconnected-(U1-PC15-Pad4)
- U1 pad 5: GND -> /mcu & adc/HSE
- U1 pad 6: /mcu & adc/ADCCS -> unconnected-(U1-PF1-Pad6)
- U1 pad 7: /mcu & adc/MOSI -> /connectors/NRST
- U1 pad 8: /mcu & adc/SCLK -> unconnected-(U1-PC0-Pad8)
- U1 pad 9: /mcu & adc/MISO -> /connectors/UART_TX_PROG
- U10 pad 1: GND -> +7V0
- U10 pad 2: Net-(U10-SW) -> GND
- U10 pad 3: Net-(U10-VIN) -> +5V0A
- U12 pad 1: GND -> +15V0A
- U12 pad 2: Net-(U12-SW) -> GND
- U12 pad 3: Net-(U12-VIN) -> GND
- U12 pad 4: Net-(U12-FB) -> Net-(U12-NC_1)
- U12 pad 5: Net-(U12-EN) -> Net-(U12-NC_1)
- U12 pad 6: Net-(U12-BOOT) -> GND
- U13 pad 1: +7V0 -> -15V0A
- U13 pad 2: GND -> -18V0
- U13 pad 3: +5V0A -> -18V0
- U14 pad 1: GND -> +3V3A
- U14 pad 2: GND -> +1V5A
- U14 pad 3: Net-(U14-VCC) -> GND
- U15 pad 1: GND -> +5V0A
- U15 pad 2: +3V3A -> +3V0A
- U15 pad 3: +7V0 -> GND
- U16 pad 1: GND -> unconnected-(U16-Pad1)
- U16 pad 2: +3V3 -> GND
- U16 pad 3: +7V0 -> /connectors/SWDIO
- U17 pad 1: /connectors/NRST -> /connectors/UART_RX_PROG
- U17 pad 3: /connectors/SWO -> unconnected-(U17-Pad3)
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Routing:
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- added copper zone on F.Cu, net +12V0A
- added copper zone on F.Cu, net +15V0
- added copper zone on F.Cu, net +15V0A
- added copper zone on F.Cu, net +15V0F
- added copper zone on F.Cu, net +18V0
- added copper zone on F.Cu, net +1V5A
- added copper zone on F.Cu, net +24V0
- added copper zone on F.Cu, net +3V0A
- added copper zone on F.Cu, net +3V3
- added copper zone on F.Cu, net +3V3A
- added copper zone on F.Cu, net +5V0A
- added copper zone on F.Cu, net +7V0
- added copper zone on F.Cu, net -15V0A
- added copper zone on F.Cu, net -18V0
- added copper zone on F.Cu, net GND
- added copper zone on In1.Cu, net GND
- added copper zone on In4.Cu, net GND
- added copper zone on In1.Cu, net GND_ISO
- added copper zone on F.Cu, net Net-(D1-A)
- added copper zone on F.Cu, net Net-(D2-A)
- added copper zone on F.Cu, net Net-(U5-BOOT)
- added copper zone on F.Cu, net Net-(U5-SW)
- added copper zone on B.Cu, net Net-(U5-VIN)
- added copper zone on F.Cu, net Net-(U5-VIN)
- added copper zone on F.Cu, net Net-(U6-SW)
- added copper zone on F.Cu, net Net-(U6-VIN)
- added copper zone on F.Cu, net Net-(U7-SW2)
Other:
- board outline added: 70 x 135 mm
- copper layers 2 -> 6
- board text added: "12V"
- board text added: "5V"
- board text added: "A1N"
- board text added: "A1P"
- board text added: "A2N"
- board text added: "A2P"
- board text added: "A3N"
- board text added: "A3P"
- board text added: "A4N"
- board text added: "A4P"
- board text added: "A5N"
- board text added: "A5P"
- board text added: "A6N"
- board text added: "A6P"
- board text added: "A7N"
- board text added: "A7P"
- board text added: "A8N"
- board text added: "A8P"
- board text added: "C40"
- board text added: "C45"
- board text added: "C51"
- board text added: "C_H"
- board text added: "C_L"
- board text added: "GND"
- board text added: "ISOLATED"
- board text added: "Marcin Trzmiel"
- board text added: "Measurement Board Rev.: 1.0"
- board text added: "STACKUP: 1. SIGNAL / POWER 2. GND 3. SIGNAL 4. SIGNAL 5. GND 6. SIGNAL / POWER"
- board text added: "U10"
- board text added: "U12"
- board text added: "U9"
- board text added: "VCC"
